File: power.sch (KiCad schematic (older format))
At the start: 26 parts, among them J3 EXT_PWR, J4 V_ORBITTY, J5 V_HUB, J6 PWR_SWITCH, Q2 Q_PMOS_GDS, U1 TL7702A, U5 P783F-Q24-S5-S

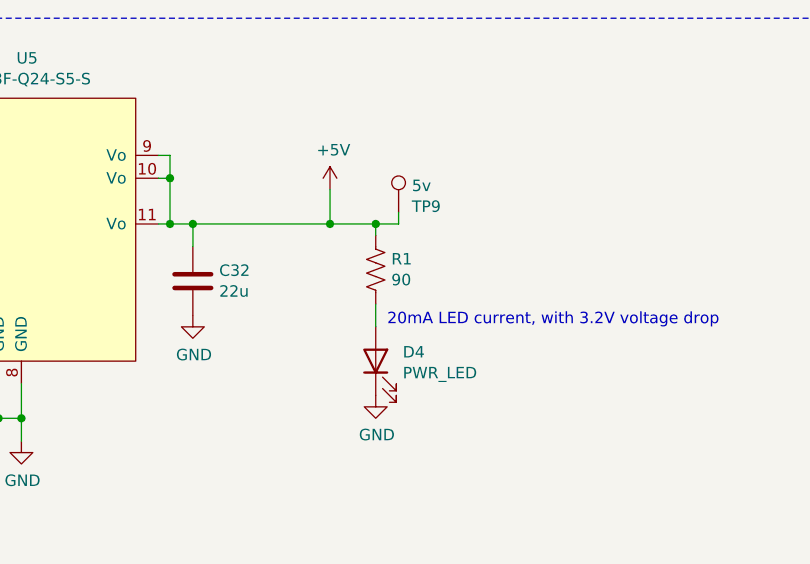
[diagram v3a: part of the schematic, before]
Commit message: Added logo to PCB. Changed resistance to preferred value.
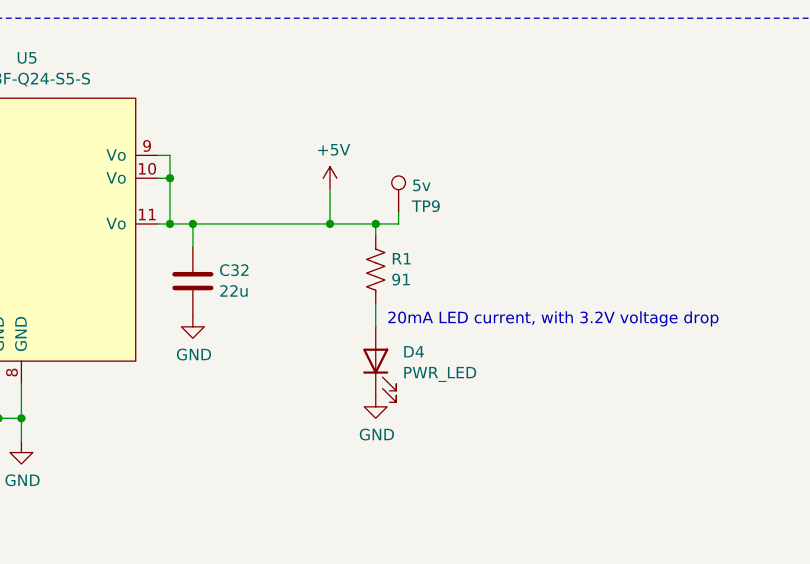
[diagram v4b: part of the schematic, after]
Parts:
- R1: value 90 -> 91
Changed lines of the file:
@@
 P 9200 1700
 F 0 "R1" H 9268 1746 50  0000 L CNN
-F 1 "90" H 9268 1655 50  0000 L CNN
+F 1 "91" H 9268 1655 50  0000 L CNN
 F 2 "Resistor_SMD:R_1206_3216Metric_Pad1.30x1.75mm_HandSolder" V 9240 1690 50  0001 C CNN
 F 3 "~" H 9200 1700 50  0001 C CNN
